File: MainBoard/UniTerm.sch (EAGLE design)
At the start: 14 parts, among them IC1 STM32F030C

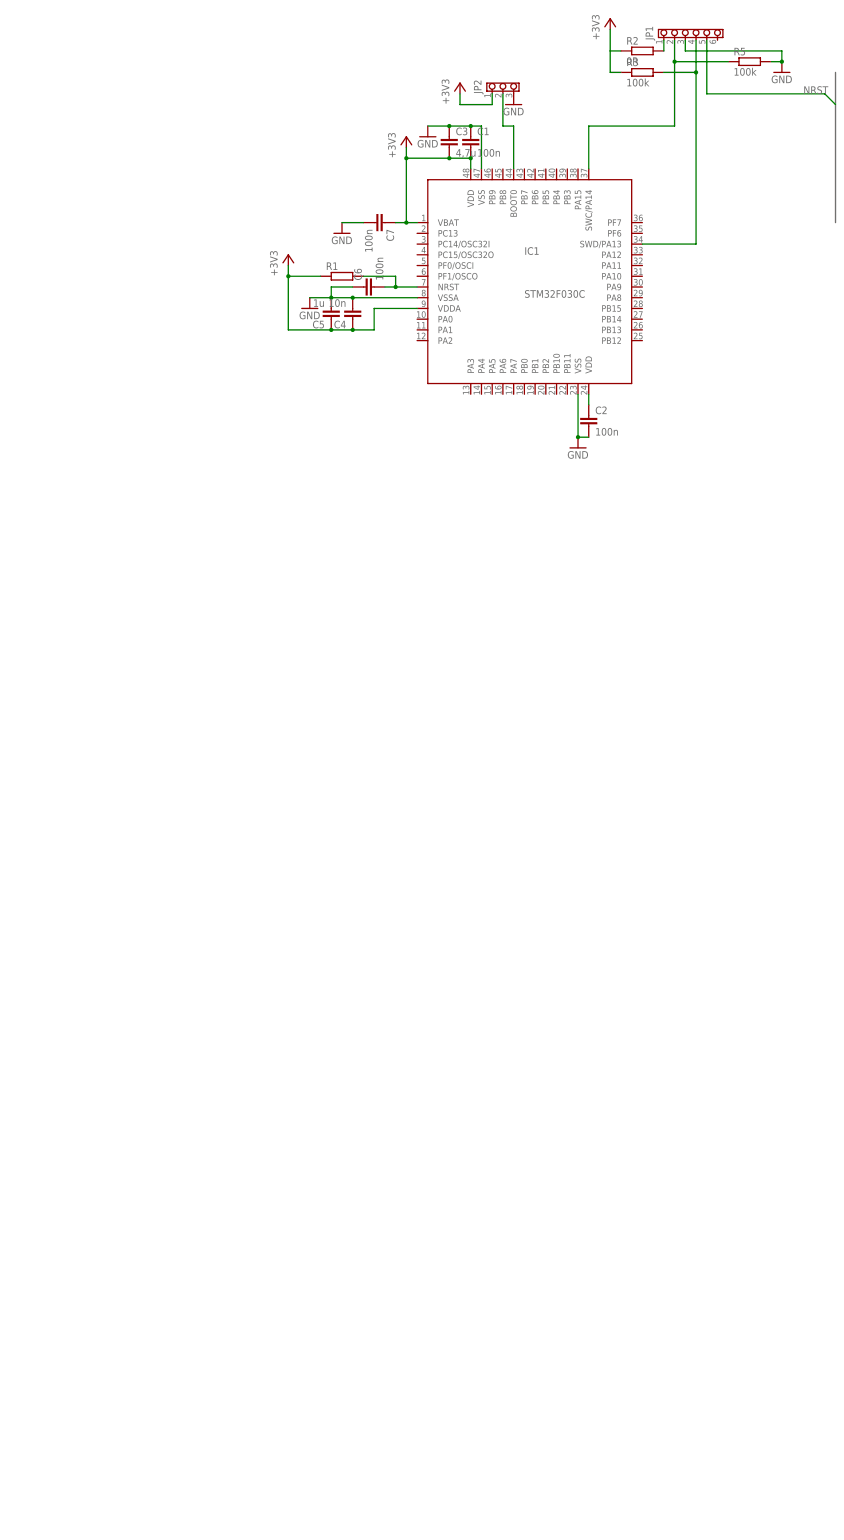
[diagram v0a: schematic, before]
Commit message: Add power switch schematic
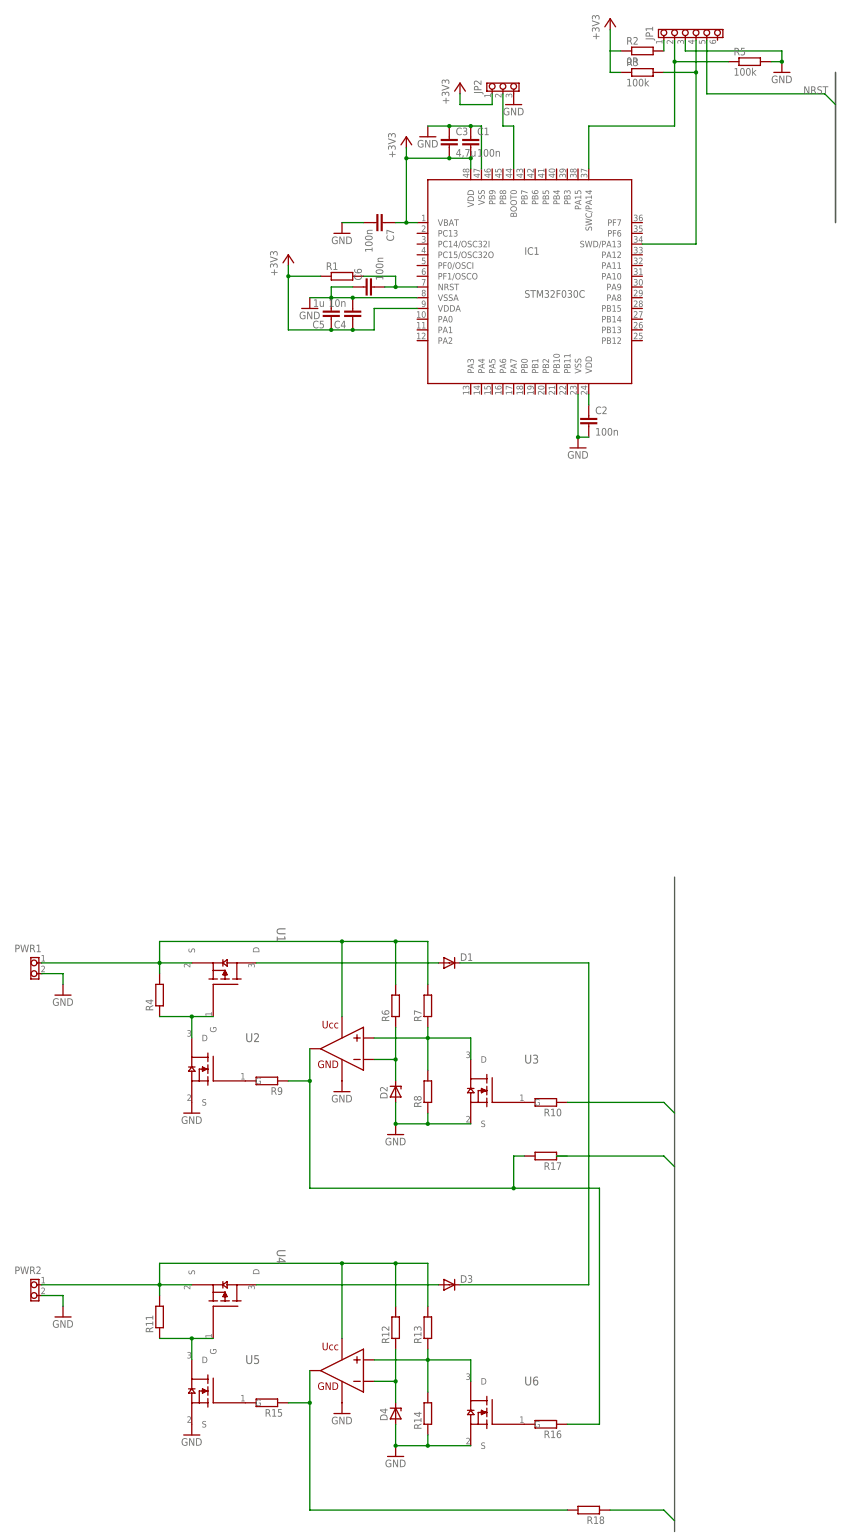
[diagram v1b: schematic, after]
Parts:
- added D1, D3: MBR0520LT, diode:MBR0520LT
- added D2, D4: (no value), diode:ZENER-DIODESMB
- added PWR1, PWR2: (no value), !pinhead:PINHD-1X2_508_H
- added R10, R11, R12, R13, R14, R15, R16, R17, R18, R4, R6, R7, R8, R9: (no value), rcl:R-EU_R1206
- added U$1, U$2: SOIC8_OZ, OZ:SOIC8_OZ
- added U1, U4: TSM2311CX, Mosfets:TSM2311CX
- added U2, U3, U5, U6: BSS138BK, Mosfets:BSS138BK
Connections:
- new net N$10: R10.2, U3.G
- new net N$11: R16.1, R17.2, R9.1, U$1A.P$A_OUT
- new net N$12: D2.C, R6.1, U$1A.P$A-
- new net N$13: R7.1, R8.2, U$1A.P$A+, U3.D
- new net N$14: R9.2, U2.G
- new net N$15: PWR2.1, R11.2, R12.2, R13.2, U$2A.P$UCC, U4.S
- new net N$16: R11.1, U4.G, U5.D
- new net N$17: D3.A, U4.D
- new net N$18: R15.1, R18.2, U$2A.P$A_OUT
- new net N$19: D4.C, R12.1, U$2A.P$A-
- new net N$20: R13.1, R14.2, U$2A.P$A+, U6.D
- new net N$21: R15.2, U5.G
- new net N$22: R16.2, U6.G
- new net N$23: D1.C, D3.C
- new net N$4: PWR1.1, R4.2, R6.2, R7.2, U$1A.P$UCC, U1.S
- new net N$6: R4.1, U1.G, U2.D
- new net N$9: D1.A, U1.D
- new net PWR2_EN: R18.1
- new net PWR_CHANGE: R10.1
- net GND: now also D2.A, D4.A, PWR1.2, PWR2.2, R14.1, R8.1, U$1A.P$GND, U$2A.P$GND, U2.S, U3.S, U5.S, U6.S

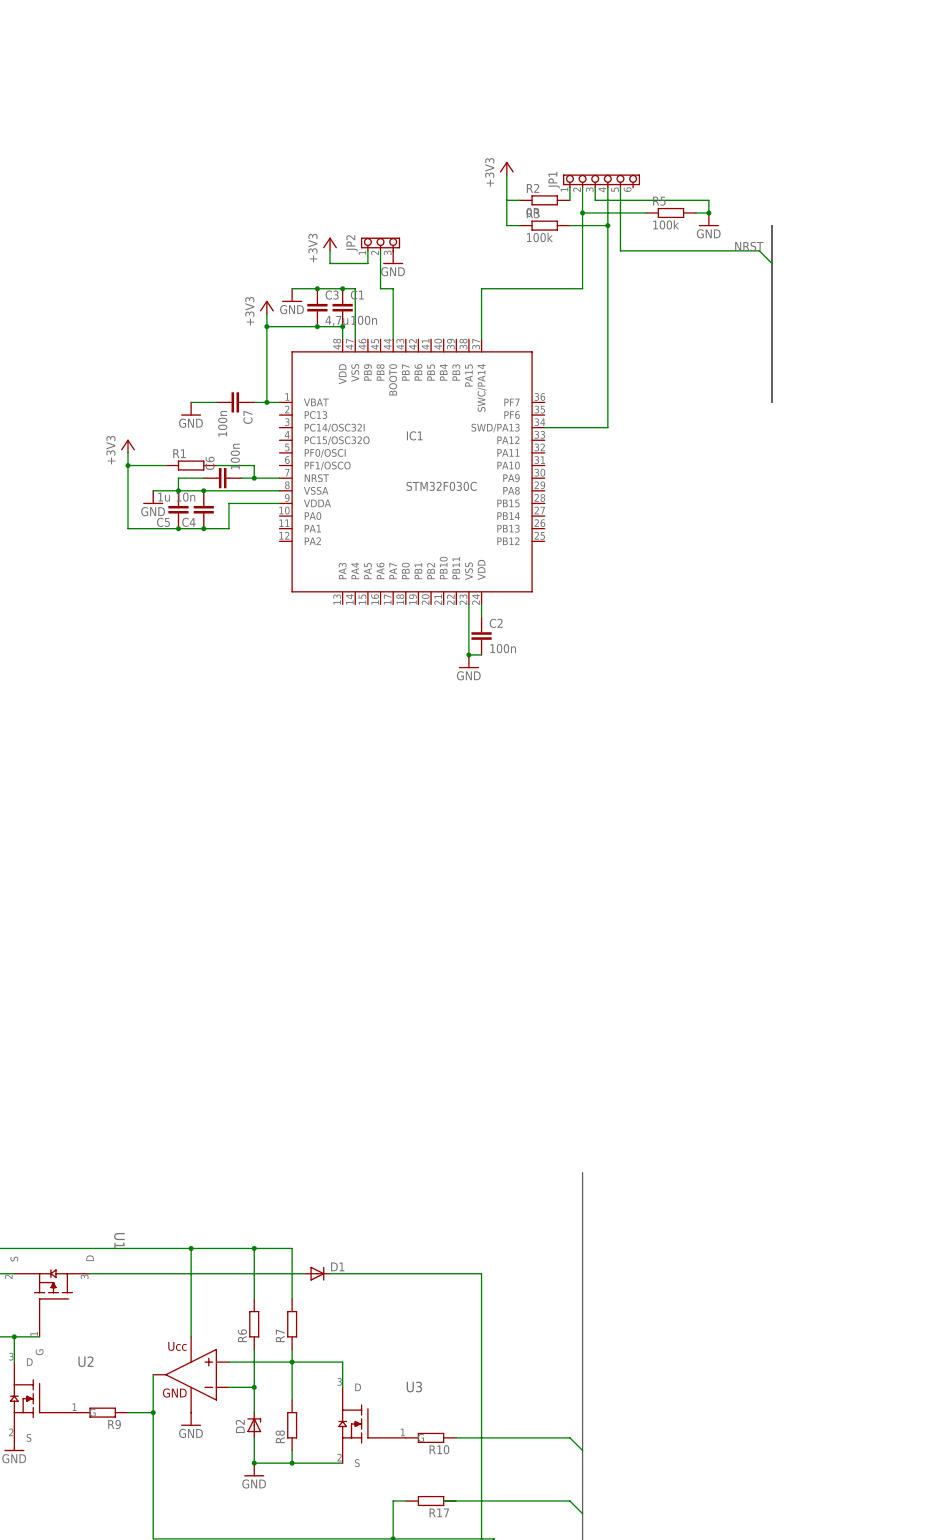
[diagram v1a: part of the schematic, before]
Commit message: Added conectors for: nRF and Front board
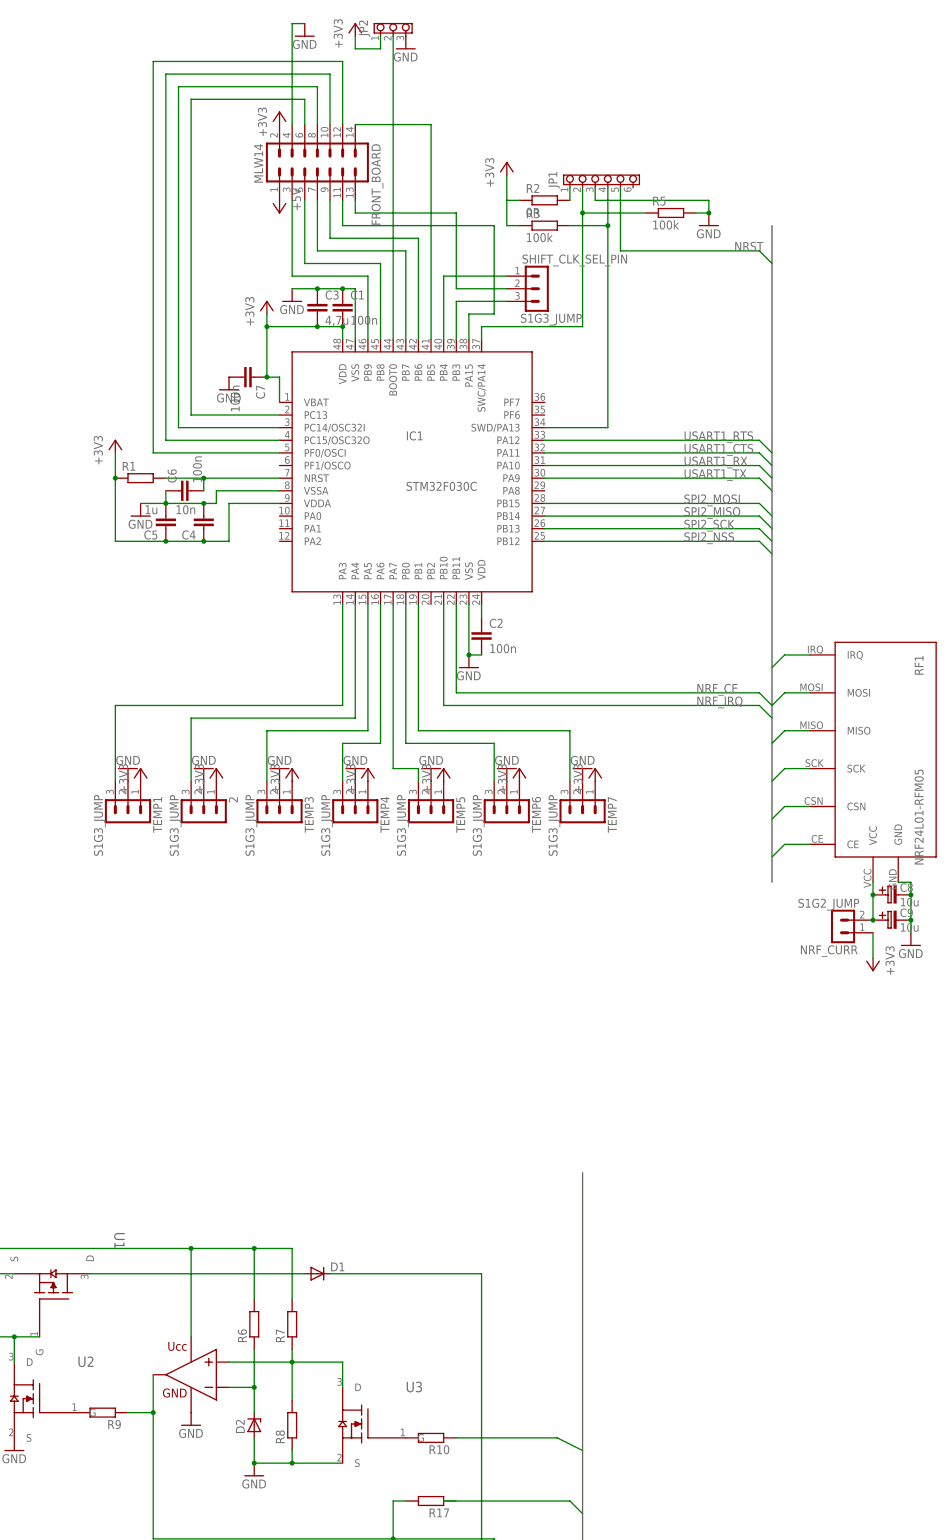
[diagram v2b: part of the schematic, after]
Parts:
- added 2, SHIFT_CLK_SEL_PIN, TEMP1, TEMP3, TEMP4, TEMP5, TEMP6, TEMP7: S1G3_JUMP, #PaJa_konektory:S1G3_JUMP
- added C8, C9: 10u, #PaJa_30:C-ELEKTROLYT_5
- added FRONT_BOARD: MLW14, #PaJa_konektory:MLW14
- added NRF_CURR: S1G2_JUMP, #PaJa_konektory:S1G2_JUMP
- added RF1: NRF24L01-RFM05, kumen:NRF24L01-RFM05
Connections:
- new net N$24: FRONT_BOARD.14, IC1.PB5
- new net N$25: FRONT_BOARD.13, SHIFT_CLK_SEL_PIN.2
- new net N$26: FRONT_BOARD.11, IC1.PA15
- new net N$27: FRONT_BOARD.9, IC1.PB6
- new net N$28: FRONT_BOARD.7, IC1.PB7
- new net N$29: FRONT_BOARD.5, IC1.PB8
- new net N$30: FRONT_BOARD.3, IC1.PB9
- new net N$31: IC1.PB4, SHIFT_CLK_SEL_PIN.1
- new net N$32: IC1.PB3, SHIFT_CLK_SEL_PIN.3
- new net N$33: FRONT_BOARD.12, IC1.PF0/OSCI
- new net N$34: FRONT_BOARD.10, IC1.PC15/OSC32O
- new net N$35: FRONT_BOARD.8, IC1.PC14/OSC32I
- new net N$36: FRONT_BOARD.6, IC1.PC13
- new net N$37: IC1.PB1, TEMP7.3
- new net N$38: IC1.PB0, TEMP6.3
- new net N$39: IC1.PA7, TEMP5.3
- new net N$40: IC1.PA6, TEMP4.3
- new net N$41: IC1.PA5, TEMP3.3
- new net N$42: 2.3, IC1.PA4
- new net N$43: IC1.PA3, TEMP1.3
- new net N$44: C8.C_EL+, C9.C_EL+, NRF_CURR.2, RF1.VCC
- new net NRF_CE: IC1.PB11, RF1.CE
- new net NRF_IRQ: IC1.PB10, RF1.IRQ
- new net SPI2_MISO: IC1.PB14, RF1.MISO
- new net SPI2_MOSI: IC1.PB15, RF1.MOSI
- new net SPI2_NSS: IC1.PB12, RF1.CSN
- new net SPI2_SCK: IC1.PB13, RF1.SCK
- new net USART1_CTS: IC1.PA11
- new net USART1_RTS: IC1.PA12
- new net USART1_RX: IC1.PA10
- new net USART1_TX: IC1.PA9
- net +3V3: now also 2.1, FRONT_BOARD.1, FRONT_BOARD.2, NRF_CURR.1, TEMP1.1, TEMP3.1, TEMP4.1, TEMP5.1, TEMP6.1, TEMP7.1
- net GND: now also 2.2, C8.C_EL-, C9.C_EL-, FRONT_BOARD.4, RF1.GND, TEMP1.2, TEMP3.2, TEMP4.2, TEMP5.2, TEMP6.2, TEMP7.2
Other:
- moved on the sheet: C4, C5, C6, C7, JP2, R1
